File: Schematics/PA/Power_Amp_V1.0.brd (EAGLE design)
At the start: 50.5 x 76.8 mm, 102 parts, among them J1 4_PIN_AMPCONN, J12 1725724, J13 1725724, J14 1725724, J2 1984633, J3 2TERMINAL_SPEAKER, J4 2TERMINAL_SPEAKER, J5 2TERMINAL_SPEAKER, U1 LME49830, U2 LME49830, U3 LME49830

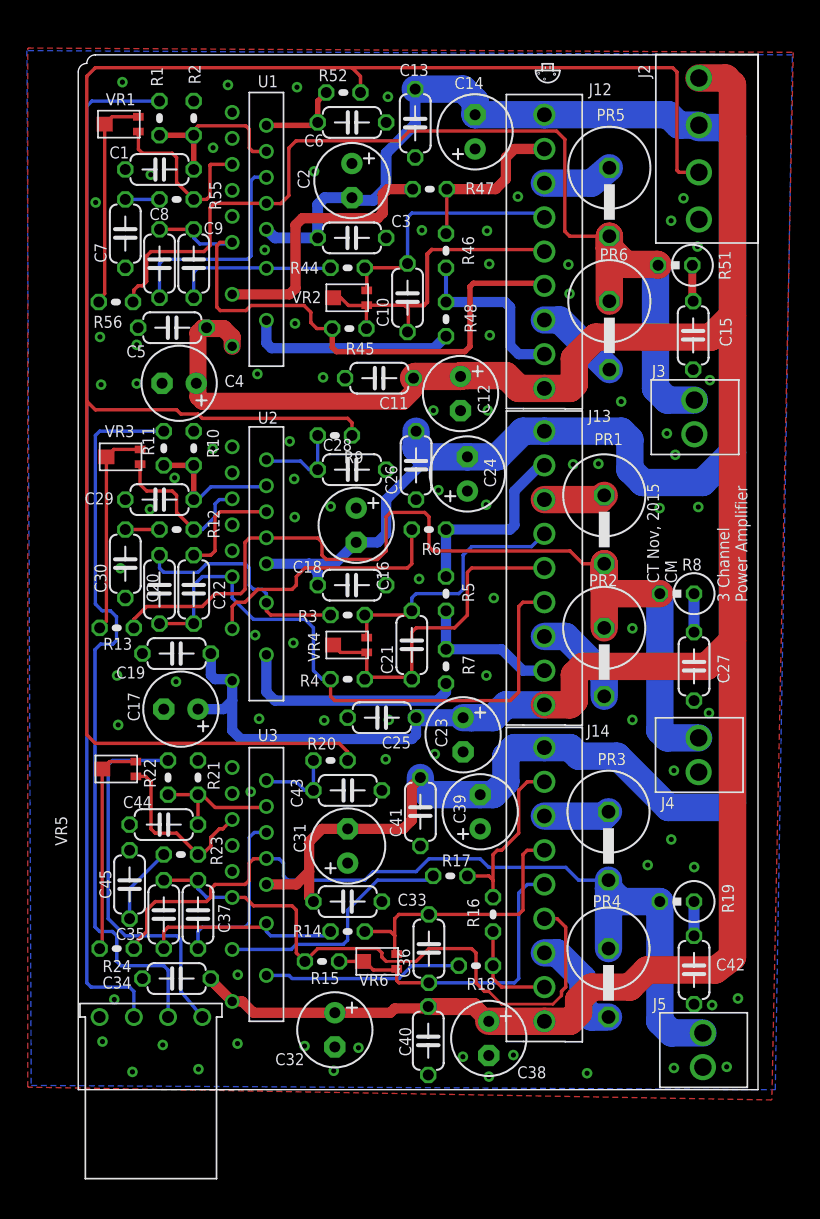
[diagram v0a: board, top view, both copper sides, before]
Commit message: small changes to my PA
t&bstop on power traces
moved 2 pin screw terminal
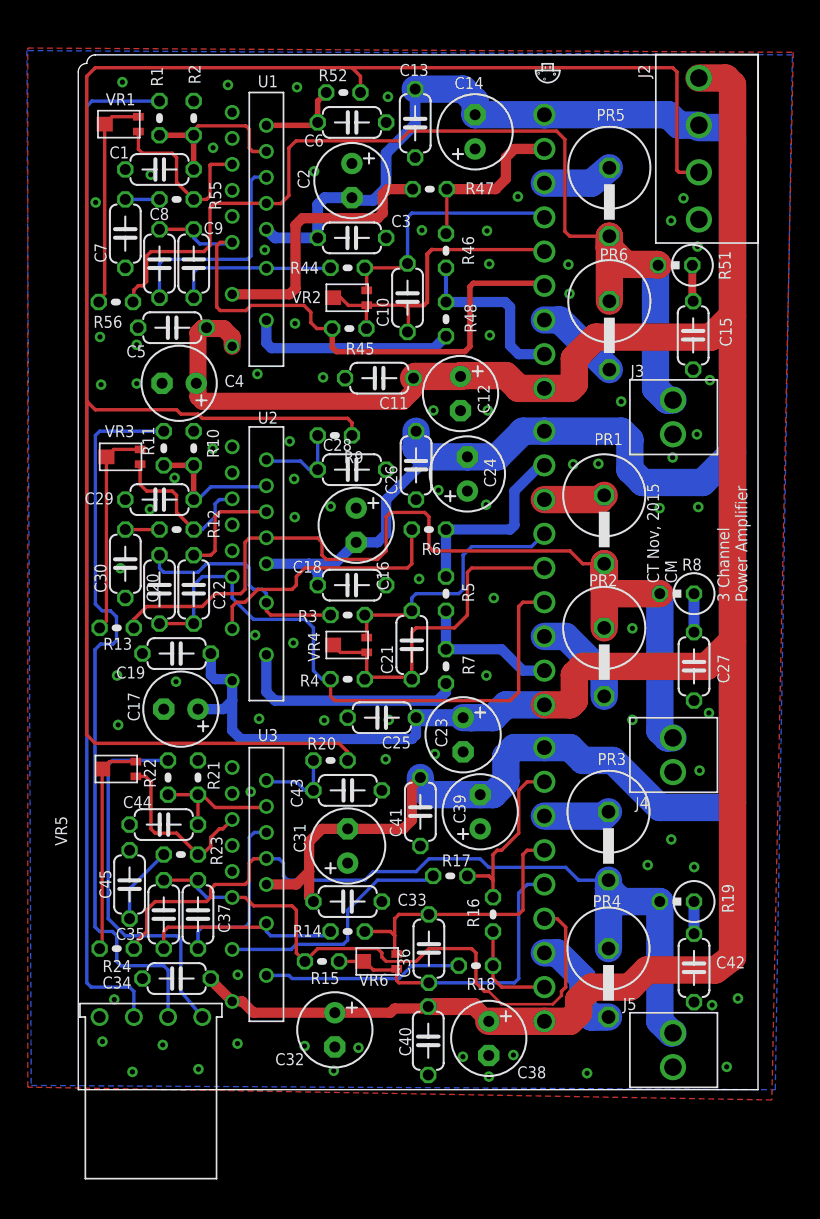
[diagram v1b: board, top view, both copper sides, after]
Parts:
- moved J5 2.22 mm to (41.0, 5.71)
- moved J4 1.90 mm to (41.0, 27.6)
- moved J3 1.59 mm to (41.0, 52.7)
- moved C42 0.15 mm to (45.7, 9.04)
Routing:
- net N$77: track 64.5 -> 62.3 mm
- net N$12: track 71.4 -> 69.4 mm
- net N$75: track 81.5 -> 79.9 mm

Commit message: added bstop and some silk screen
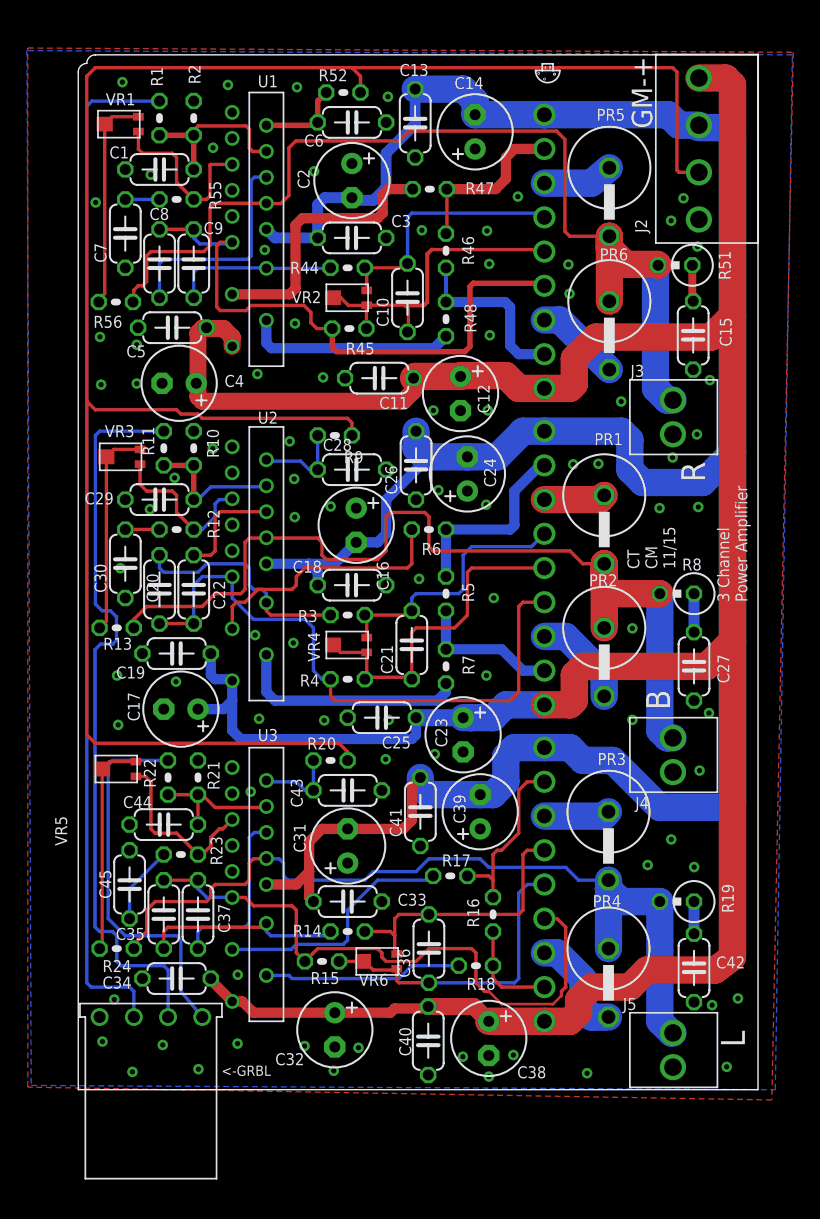
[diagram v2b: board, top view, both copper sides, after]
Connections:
- net LEFT renamed LEFT_IN
- net N$1 renamed BASS_IN
- net N$12 renamed BASS_OUT
- net N$75 renamed RIGHT_OUT
- net N$77 renamed LEFT_OUT
- net RIGHT renamed RIGHT_IN
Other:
- board text added: "<-GRBL"
- board text added: "B"
- board text added: "CT CM 11/15"
- board text added: "GM-+"
- board text added: "L"
- board text added: "R"
- board text removed: "CT Nov, 2015 CM"
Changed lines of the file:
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@@
 <?xml version="1.0" encoding="utf-8"?>
 <!DOCTYPE eagle SYSTEM "eagle.dtd">
-<eagle version="7.4.0">
+<eagle version="6.5.0">
 <drawing>
 <settings>
@@
 <text x="49.6775875" y="36.208928125" size="0.889" layer="21" font="vector" ratio="15" rot="R90">3 Channel
 Power Amplifier</text>
-<text x="44.455865625" y="37.606578125" size="0.889" layer="21" font="vector" ratio="15" rot="R90">CT Nov, 2015
-CM</text>
+<text x="44.327909375" y="38.657965625" size="0.889" layer="21" font="vector" ratio="15" rot="R90">CT
+CM
+11/15</text>
 <wire x1="46.05363125" y1="75.085840625" x2="48.098665625" y2="75.071165625" width="2.159" layer="29"/>
 <wire x1="48.098665625" y1="75.071165625" x2="48.5856625" y2="74.584178125" width="2.159" layer="29"/>
@@
 <wire x1="41.865125" y1="45.099946875" x2="46.329528125" y2="45.048578125" width="2.159" layer="30"/>
 <wire x1="46.329528125" y1="45.048578125" x2="48.4747" y2="47.19375" width="2.159" layer="30"/>
+<wire x1="39.456296875" y1="58.552646875" x2="39.428890625" y2="58.552646875" width="2.159" layer="29"/>
+<wire x1="39.428890625" y1="58.552646875" x2="39.428890625" y2="63.3081625" width="2.159" layer="29"/>
+<wire x1="42.819446875" y1="61.244359375" x2="39.75700625" y2="61.244359375" width="2.159" layer="29"/>
+<wire x1="39.75700625" y1="61.244359375" x2="39.75700625" y2="61.27169375" width="2.159" layer="29"/>
+<wire x1="43.112609375" y1="36.844546875" x2="39.137365625" y2="36.844546875" width="2.159" layer="29"/>
+<wire x1="39.137365625" y1="36.844546875" x2="39.137365625" y2="36.890103125" width="2.159" layer="29"/>
+<wire x1="39.03485" y1="34.3275" x2="39.046240625" y2="34.3275" width="2.159" layer="29"/>
+<wire x1="39.046240625" y1="34.3275" x2="39.046240625" y2="38.97435625" width="2.159" layer="29"/>
+<wire x1="34.630159375" y1="43.83188125" x2="38.75898125" y2="43.83188125" width="2.032" layer="29"/>
+<wire x1="38.75898125" y1="43.83188125" x2="38.75898125" y2="43.859215625" width="2.032" layer="29"/>
+<wire x1="39.412440625" y1="5.428921875" x2="38.11619375" y2="5.428921875" width="2.032" layer="30"/>
+<wire x1="38.11619375" y1="5.428921875" x2="38.11619375" y2="5.5929375" width="2.032" layer="30"/>
+<wire x1="37.54190625" y1="8.053175" x2="37.492684375" y2="8.053175" width="2.032" layer="30"/>
+<wire x1="37.492684375" y1="8.053175" x2="37.492684375" y2="5.986575" width="2.032" layer="30"/>
+<wire x1="34.575615625" y1="10.214671875" x2="35.287428125" y2="10.214671875" width="2.032" layer="30"/>
+<wire x1="35.287428125" y1="10.214671875" x2="35.287428125" y2="10.1553625" width="2.032" layer="30"/>
+<wire x1="34.774846875" y1="10.136521875" x2="35.504015625" y2="10.136521875" width="2.032" layer="30"/>
+<wire x1="35.504015625" y1="10.136521875" x2="37.5541" y2="8.0864375" width="2.032" layer="30"/>
+<wire x1="43.940515625" y1="4.2506125" x2="43.940515625" y2="4.42808125" width="2.032" layer="30"/>
+<wire x1="43.940515625" y1="4.42808125" x2="43.22959375" y2="5.139003125" width="2.032" layer="30"/>
+<wire x1="43.22959375" y1="5.139003125" x2="43.22959375" y2="13.848071875" width="2.032" layer="30"/>
+<wire x1="43.22959375" y1="13.848071875" x2="43.15594375" y2="13.921721875" width="2.032" layer="30"/>
+<wire x1="43.15594375" y1="13.921721875" x2="39.34053125" y2="13.921721875" width="2.032" layer="30"/>
+<wire x1="39.34053125" y1="13.921721875" x2="39.331040625" y2="13.9312125" width="2.032" layer="30"/>
+<wire x1="39.331040625" y1="13.9312125" x2="39.331040625" y2="10.48636875" width="2.032" layer="30"/>
+<wire x1="39.331040625" y1="10.48636875" x2="39.350021875" y2="10.4673875" width="2.032" layer="30"/>
+<wire x1="39.350021875" y1="10.4673875" x2="39.350021875" y2="15.49714375" width="2.032" layer="30"/>
+<wire x1="39.350021875" y1="15.49714375" x2="39.365171875" y2="15.51229375" width="2.032" layer="30"/>
+<wire x1="34.991265625" y1="20.3186" x2="39.069046875" y2="20.3186" width="2.032" layer="30"/>
+<wire x1="39.069046875" y1="20.3186" x2="39.342390625" y2="20.59194375" width="2.032" layer="30"/>
+<wire x1="44.090903125" y1="26.214390625" x2="43.694303125" y2="26.214390625" width="2.032" layer="30"/>
+<wire x1="43.694303125" y1="26.214390625" x2="43.270609375" y2="26.638084375" width="2.032" layer="30"/>
+<wire x1="43.270609375" y1="26.638084375" x2="43.270609375" y2="36.777675" width="2.032" layer="30"/>
+<wire x1="43.270609375" y1="36.777675" x2="43.24929375" y2="36.798990625" width="2.032" layer="30"/>
+<wire x1="39.05763125" y1="29.452859375" x2="39.05763125" y2="30.76263125" width="2.032" layer="30"/>
+<wire x1="39.05763125" y1="30.76263125" x2="39.03485" y2="30.7854125" width="2.032" layer="30"/>
+<wire x1="39.03485" y1="30.7854125" x2="39.03485" y2="30.80595625" width="2.032" layer="30"/>
+<wire x1="39.03485" y1="30.80595625" x2="36.215421875" y2="33.625384375" width="2.032" layer="30"/>
+<wire x1="36.215421875" y1="33.625384375" x2="34.673159375" y2="33.625384375" width="2.032" layer="30"/>
+<wire x1="34.673159375" y1="33.625384375" x2="34.665253125" y2="33.633290625" width="2.032" layer="30"/>
+<wire x1="28.76504375" y1="27.649484375" x2="30.8297375" y2="27.649484375" width="2.032" layer="30"/>
+<wire x1="30.8297375" y1="27.649484375" x2="31.786465625" y2="28.6062125" width="2.032" layer="30"/>
+<wire x1="31.786465625" y1="28.6062125" x2="34.425090625" y2="28.6062125" width="2.032" layer="30"/>
+<wire x1="34.425090625" y1="28.6062125" x2="34.43875625" y2="28.592546875" width="2.032" layer="30"/>
+<wire x1="39.44525625" y1="53.469134375" x2="39.443790625" y2="53.469134375" width="2.032" layer="30"/>
+<wire x1="39.443790625" y1="53.469134375" x2="35.802640625" y2="57.110284375" width="2.032" layer="30"/>
+<wire x1="35.802640625" y1="57.110284375" x2="34.70328125" y2="57.110284375" width="2.032" layer="30"/>
+<wire x1="34.70328125" y1="57.110284375" x2="34.670478125" y2="57.1430875" width="2.032" layer="30"/>
+<wire x1="43.867775" y1="51.226625" x2="43.75378125" y2="51.226625" width="2.032" layer="30"/>
+<wire x1="43.75378125" y1="51.226625" x2="42.909178125" y2="52.071228125" width="2.032" layer="30"/>
+<wire x1="42.909178125" y1="52.071228125" x2="42.909178125" y2="61.11535625" width="2.032" layer="30"/>
+<wire x1="42.909178125" y1="61.11535625" x2="42.997178125" y2="61.20335625" width="2.032" layer="30"/>
+<wire x1="34.7848125" y1="67.302559375" x2="38.268178125" y2="67.302559375" width="2.032" layer="30"/>
+<wire x1="38.268178125" y1="67.302559375" x2="39.397478125" y2="68.431859375" width="2.032" layer="30"/>
+<text x="10.633434375" y="1.030003125" size="0.762" layer="21">&lt;-GRBL</text>
+<text x="42.618134375" y="71.365584375" size="1.524" layer="21" rot="R90">GM-+</text>
+<text x="49.4960125" y="3.1652375" size="1.778" layer="21" rot="R90">L</text>
+<text x="43.940765625" y="28.18754375" size="1.778" layer="21" rot="R90">B</text>
+<text x="46.546840625" y="45.110309375" size="1.778" layer="21" rot="R90">R</text>
 </plain>
 <attributes>
@@
 <pass name="Default">
 <param name="RoutingGrid" value="50mil"/>
-<param name="AutoGrid" value="1"/>
-<param name="Efforts" value="0"/>
-<param name="TopRouterVariant" value="1"/>
 <param name="tpViaShape" value="round"/>
 <param name="PrefDir.1" value="|"/>
@@
 </element>
 <element name="J2" library="Amplifier_Parts" package="1984633" value="1984633" x="50.4825" y="62.865" smashed="yes" rot="R90">
-<attribute name="NAME" x="42.4609375" y="75.105478125" size="0.889" layer="25" font="vector" ratio="15" rot="R90"/>
+<attribute name="NAME" x="42.23409375" y="63.622340625" size="0.889" layer="25" font="vector" ratio="15" rot="R90"/>
 </element>
 <element name="J3" library="Amplifier_Parts" package="2TERMINAL_SPEAKER" value="2TERMINAL_SPEAKER" x="40.9575" y="52.705" smashed="yes" rot="R270">
@@
 <wire x1="32.7025" y1="54.61" x2="34.6075" y2="54.61" width="0.762" layer="16"/>
 </signal>
-<signal name="N$75">
+<signal name="RIGHT_OUT">
 <contactref element="R51" pad="2"/>
 <contactref element="R56" pad="1"/>
@@
 <wire x1="29.382859375" y1="6.177140625" x2="30.48" y2="5.08" width="1.27" layer="1"/>
 </signal>
-<signal name="RIGHT">
+<signal name="RIGHT_IN">
 <contactref element="R1" pad="2"/>
 <contactref element="J1" pad="1"/>
@@
 <wire x1="0.635" y1="26.3525" x2="0.635" y2="51.1175" width="0.254" layer="1"/>
 </signal>
-<signal name="LEFT">
+<signal name="LEFT_IN">
 <contactref element="J1" pad="3"/>
 <contactref element="R22" pad="2"/>
@@
 <wire x1="7.62" y1="7.3025" x2="9.2075" y2="5.3975" width="0.254" layer="16"/>
 </signal>
-<signal name="N$77">
+<signal name="LEFT_OUT">
 <contactref element="R19" pad="2"/>
 <contactref element="R24" pad="1"/>
@@
 <wire x1="36.195" y1="33.655" x2="34.6075" y2="33.655" width="2.032" layer="16"/>
 </signal>
-<signal name="N$12">
+<signal name="BASS_OUT">
 <contactref element="R8" pad="2"/>
 <contactref element="R13" pad="1"/>
@@
 <wire x1="38.1" y1="67.31" x2="39.4335" y2="68.453" width="2.032" layer="16"/>
 </signal>
-<signal name="N$1">
+<signal name="BASS_IN">
 <contactref element="J1" pad="2"/>
 <contactref element="R11" pad="2"/>
